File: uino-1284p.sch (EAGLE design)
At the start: 59 parts, among them J1 Micro USB, J2 M03X2, J3 POWER_JACKPTH, J4 M03X2, J5 IO, U1 ATMEGA8U2AU, U2 LD117AS50TR, U3 ATMEGA1284AU, X1 16MHz, X2 16MHz

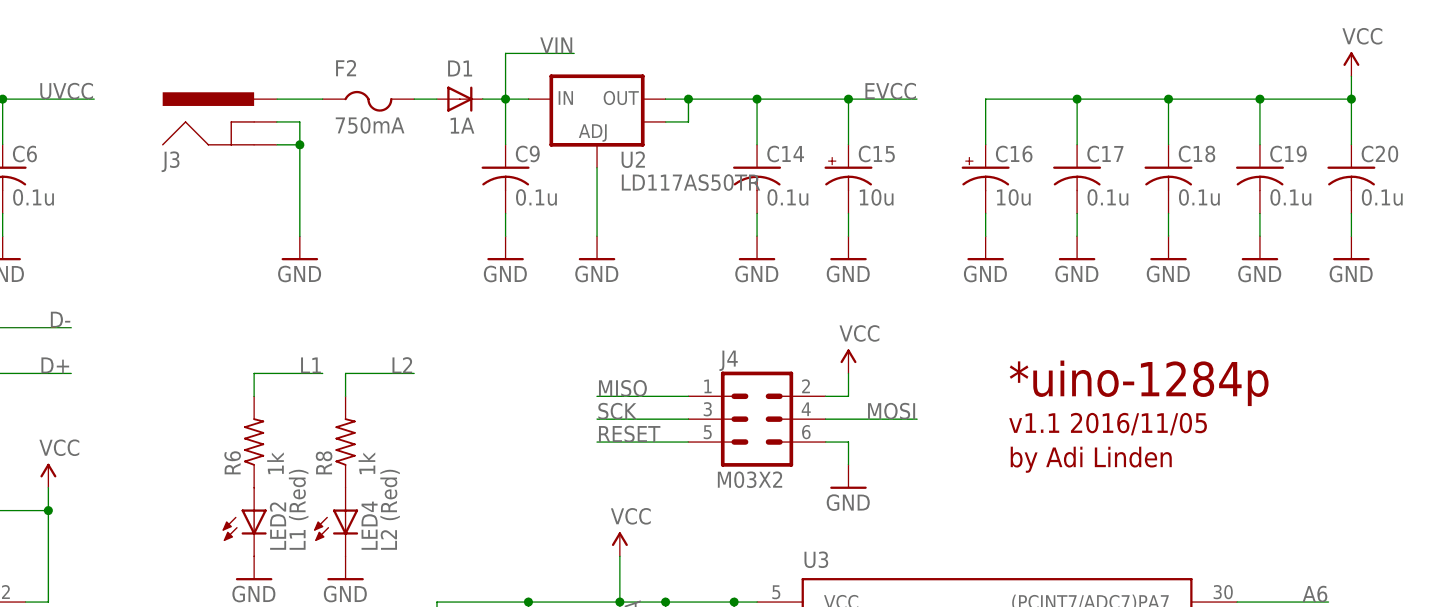
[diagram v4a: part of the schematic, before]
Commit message: Changed power input jack to screw terminal.
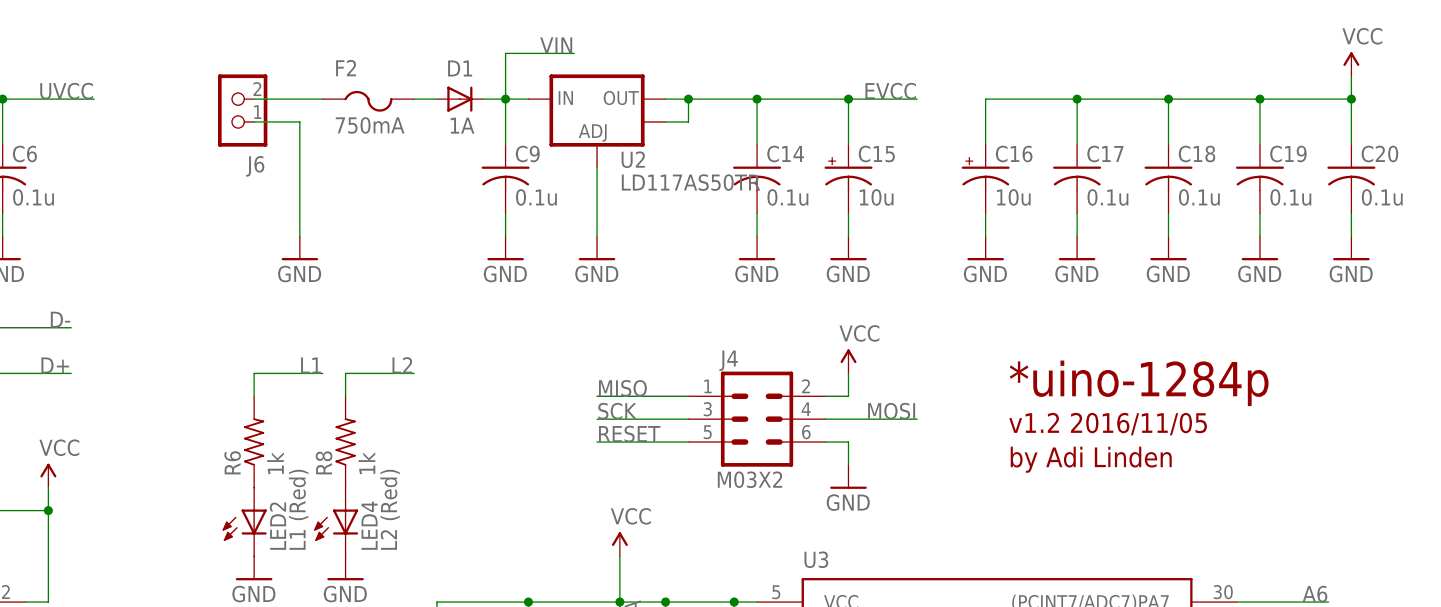
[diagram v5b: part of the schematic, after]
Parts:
- removed J3: POWER_JACKPTH, SparkFun:POWER_JACKPTH
- added J6: CON_TERMINAL_BLOCK_02-5MM, adi-misc:CON_TERMINAL_BLOCK_02-5MM
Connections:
- removed net N$25: F2.1, J3.PWR
- new net N$17: F2.1, J6.2
- net GND: now also J6.1; no longer J3.GND, J3.GNDBREAK
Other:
- note added: "v1.2 2016/11/05"
- note removed: "v1.1 2016/11/05"
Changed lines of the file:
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@@
 <part name="C7" library="rcl" deviceset="C-US" device="C0805" value="0.1u"/>
 <part name="U2" library="adi-misc" deviceset="V_REG_LM1117" device="SOT223" value="LD117AS50TR"/>
-<part name="J3" library="SparkFun" deviceset="POWER_JACK" device="PTH" value=""/>
 <part name="GND12" library="supply1" deviceset="GND" device=""/>
 <part name="GND16" library="supply1" deviceset="GND" device=""/>
@@
 <part name="C8" library="rcl" deviceset="C-US" device="C0805" value="0.1u"/>
 <part name="GND14" library="supply1" deviceset="GND" device=""/>
+<part name="J6" library="adi-misc" deviceset="CON_TERMINAL_BLOCK_02" device="-5MM"/>
 </parts>
 <sheets>
@@
 <plain>
 <text x="172.72" y="137.16" size="3.81" layer="94" ratio="18">*uino-1284p</text>
-<text x="172.72" y="133.096" size="2.1844" layer="94" ratio="12">v1.1 2016/11/05</text>
+<text x="172.72" y="133.096" size="2.1844" layer="94" ratio="12">v1.2 2016/11/05</text>
 <text x="172.72" y="129.286" size="2.1844" layer="94" ratio="12">by Adi Linden</text>
 </plain>
@@
 <instance part="C7" gate="G$1" x="88.9" y="35.56" rot="R270"/>
 <instance part="U2" gate="G$1" x="127" y="170.18"/>
-<instance part="J3" gate="G$1" x="88.9" y="162.56"/>
 <instance part="GND12" gate="1" x="93.98" y="152.4"/>
 <instance part="GND16" gate="1" x="116.84" y="152.4"/>
@@
 <instance part="C8" gate="G$1" x="109.22" y="106.68"/>
 <instance part="GND14" gate="1" x="109.22" y="96.52"/>
+<instance part="J6" gate="CON" x="88.9" y="167.64" rot="R180"/>
 </instances>
 <busses>
@@
 </segment>
 <segment>
-<wire x1="91.44" y1="167.64" x2="93.98" y2="167.64" width="0.1524" layer="91"/>
-<wire x1="93.98" y1="167.64" x2="93.98" y2="165.1" width="0.1524" layer="91"/>
-<wire x1="93.98" y1="165.1" x2="93.98" y2="154.94" width="0.1524" layer="91"/>
-<wire x1="91.44" y1="165.1" x2="93.98" y2="165.1" width="0.1524" layer="91"/>
-<junction x="93.98" y="165.1"/>
-<pinref part="J3" gate="G$1" pin="GNDBREAK"/>
+<wire x1="93.98" y1="167.64" x2="93.98" y2="154.94" width="0.1524" layer="91"/>
 <pinref part="GND12" gate="1" pin="GND"/>
-<pinref part="J3" gate="G$1" pin="GND"/>
+<pinref part="J6" gate="CON" pin="1"/>
+<wire x1="88.9" y1="167.64" x2="93.98" y2="167.64" width="0.1524" layer="91"/>
 </segment>
 <segment>
@@
 </segment>
 </net>
-<net name="N$25" class="0">
-<segment>
-<wire x1="91.44" y1="170.18" x2="96.52" y2="170.18" width="0.1524" layer="91"/>
-<pinref part="J3" gate="G$1" pin="PWR"/>
-<pinref part="F2" gate="G$1" pin="1"/>
-</segment>
-</net>
 <net name="N$34" class="0">
 <segment>
@@
 </segment>
 </net>
+<net name="N$17" class="0">
+<segment>
+<pinref part="J6" gate="CON" pin="2"/>
+<pinref part="F2" gate="G$1" pin="1"/>
+<wire x1="88.9" y1="170.18" x2="96.52" y2="170.18" width="0.1524" layer="91"/>
+</segment>
+</net>

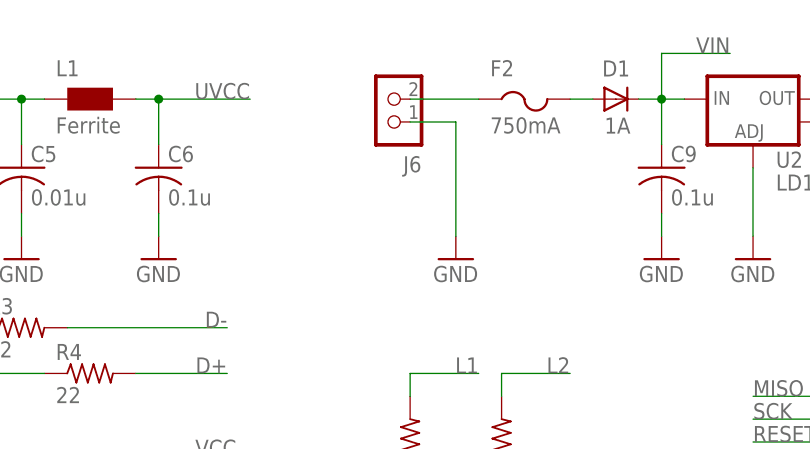
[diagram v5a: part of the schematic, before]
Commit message: Renamed power jack.
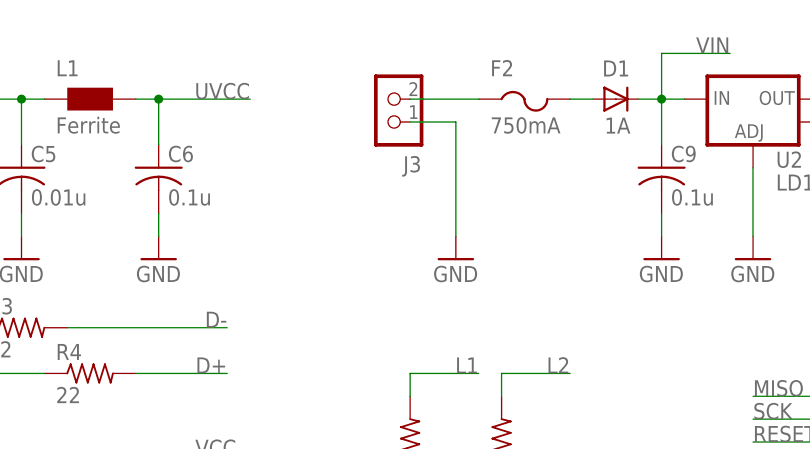
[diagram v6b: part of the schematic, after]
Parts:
- renumbered J6 to J3
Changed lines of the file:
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@@
 <part name="C8" library="rcl" deviceset="C-US" device="C0805" value="0.1u"/>
 <part name="GND14" library="supply1" deviceset="GND" device=""/>
-<part name="J6" library="adi-misc" deviceset="CON_TERMINAL_BLOCK_02" device="-5MM"/>
+<part name="J3" library="adi-misc" deviceset="CON_TERMINAL_BLOCK_02" device="-5MM"/>
 </parts>
 <sheets>
@@
 <instance part="C8" gate="G$1" x="109.22" y="106.68"/>
 <instance part="GND14" gate="1" x="109.22" y="96.52"/>
-<instance part="J6" gate="CON" x="88.9" y="167.64" rot="R180"/>
+<instance part="J3" gate="CON" x="88.9" y="167.64" rot="R180"/>
 </instances>
 <busses>
@@
 <wire x1="93.98" y1="167.64" x2="93.98" y2="154.94" width="0.1524" layer="91"/>
 <pinref part="GND12" gate="1" pin="GND"/>
-<pinref part="J6" gate="CON" pin="1"/>
+<pinref part="J3" gate="CON" pin="1"/>
 <wire x1="88.9" y1="167.64" x2="93.98" y2="167.64" width="0.1524" layer="91"/>
 </segment>
@@
 <net name="N$17" class="0">
 <segment>
-<pinref part="J6" gate="CON" pin="2"/>
+<pinref part="J3" gate="CON" pin="2"/>
 <pinref part="F2" gate="G$1" pin="1"/>
 <wire x1="88.9" y1="170.18" x2="96.52" y2="170.18" width="0.1524" layer="91"/>

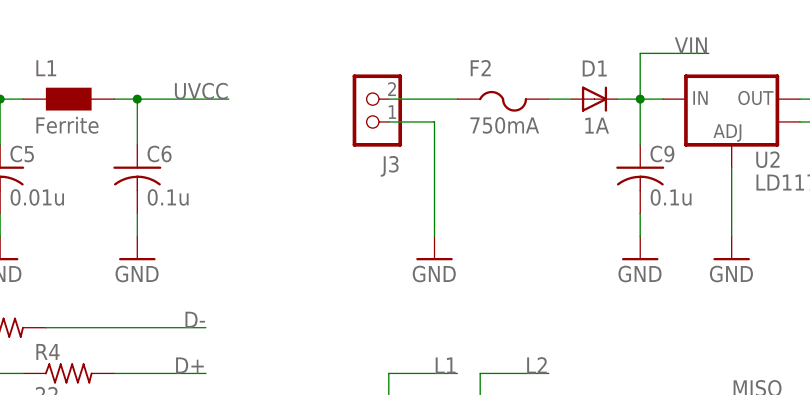
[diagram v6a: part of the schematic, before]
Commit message: Changed power jack orientation.
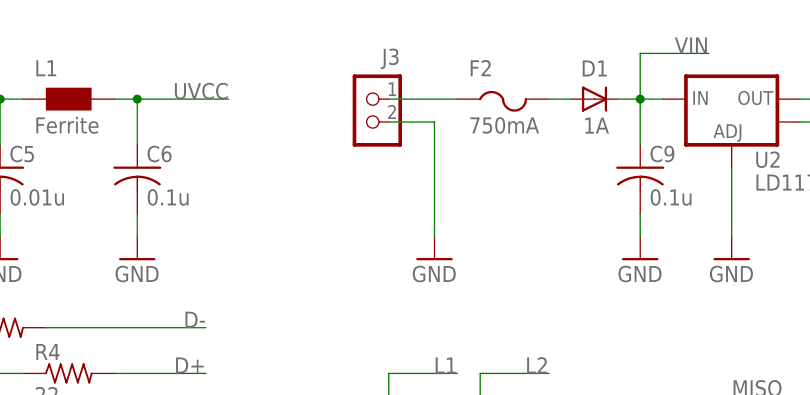
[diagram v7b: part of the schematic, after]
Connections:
- net GND: now also J3.2; no longer J3.1
- net N$17: now also J3.1; no longer J3.2
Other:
- moved on the sheet: J3
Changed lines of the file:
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@@
 <instance part="C8" gate="G$1" x="109.22" y="106.68"/>
 <instance part="GND14" gate="1" x="109.22" y="96.52"/>
-<instance part="J3" gate="CON" x="88.9" y="167.64" rot="R180"/>
+<instance part="J3" gate="CON" x="88.9" y="170.18" rot="MR0"/>
 </instances>
 <busses>
@@
 <wire x1="93.98" y1="167.64" x2="93.98" y2="154.94" width="0.1524" layer="91"/>
 <pinref part="GND12" gate="1" pin="GND"/>
-<pinref part="J3" gate="CON" pin="1"/>
-<wire x1="88.9" y1="167.64" x2="93.98" y2="167.64" width="0.1524" layer="91"/>
+<pinref part="J3" gate="CON" pin="2"/>
+<wire x1="93.98" y1="167.64" x2="88.9" y2="167.64" width="0.1524" layer="91"/>
 </segment>
 <segment>
@@
 <net name="N$17" class="0">
 <segment>
-<pinref part="J3" gate="CON" pin="2"/>
 <pinref part="F2" gate="G$1" pin="1"/>
-<wire x1="88.9" y1="170.18" x2="96.52" y2="170.18" width="0.1524" layer="91"/>
-</segment>
-</net>
+<pinref part="J3" gate="CON" pin="1"/>
+<wire x1="96.52" y1="170.18" x2="88.9" y2="170.18" width="0.1524" layer="91"/>
+</segment>
+</net>

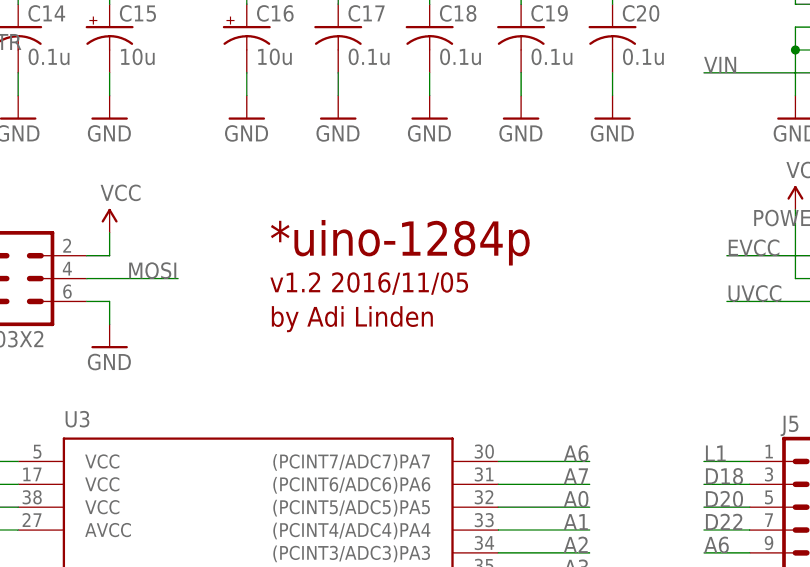
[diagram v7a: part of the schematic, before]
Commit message: Increased text sizes. Optimized polygon fills and routing.
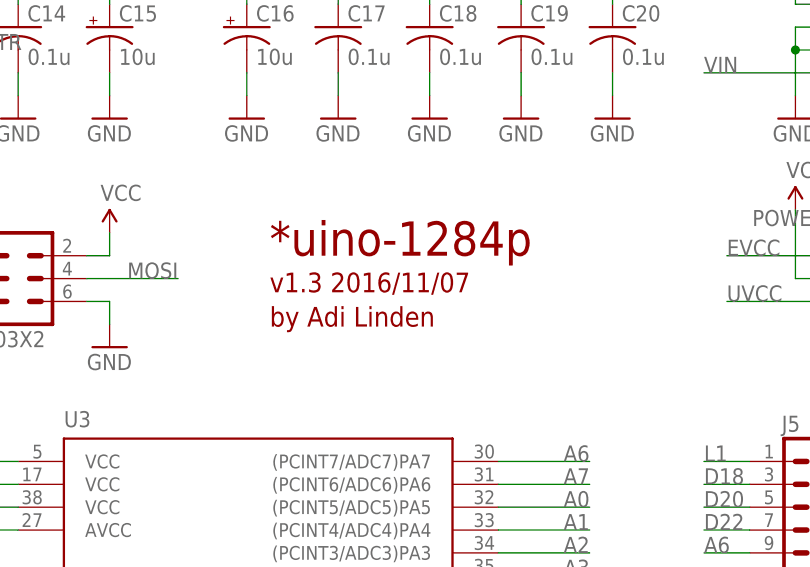
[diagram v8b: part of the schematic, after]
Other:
- note added: "v1.3 2016/11/07"
- note removed: "v1.2 2016/11/05"
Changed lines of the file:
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@@
 <plain>
 <text x="172.72" y="137.16" size="3.81" layer="94" ratio="18">*uino-1284p</text>
-<text x="172.72" y="133.096" size="2.1844" layer="94" ratio="12">v1.2 2016/11/05</text>
+<text x="172.72" y="133.096" size="2.1844" layer="94" ratio="12">v1.3 2016/11/07</text>
 <text x="172.72" y="129.286" size="2.1844" layer="94" ratio="12">by Adi Linden</text>
 </plain>
